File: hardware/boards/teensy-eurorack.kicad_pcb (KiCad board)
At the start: 2 copper layers, 64.8 x 109.2 mm, 52 parts, among them J1 Conn_01x03, J2 Conn_01x02, J27 Conn_01x02, J28 Conn_02x08_Odd_Even, J3 Conn_01x03, U2 AD5754BREZ, U3 AD5754BREZ, U4 Teensy4.1, U5 MCP1700-2502E, U6 AD7606BSTZ, U7 6N138

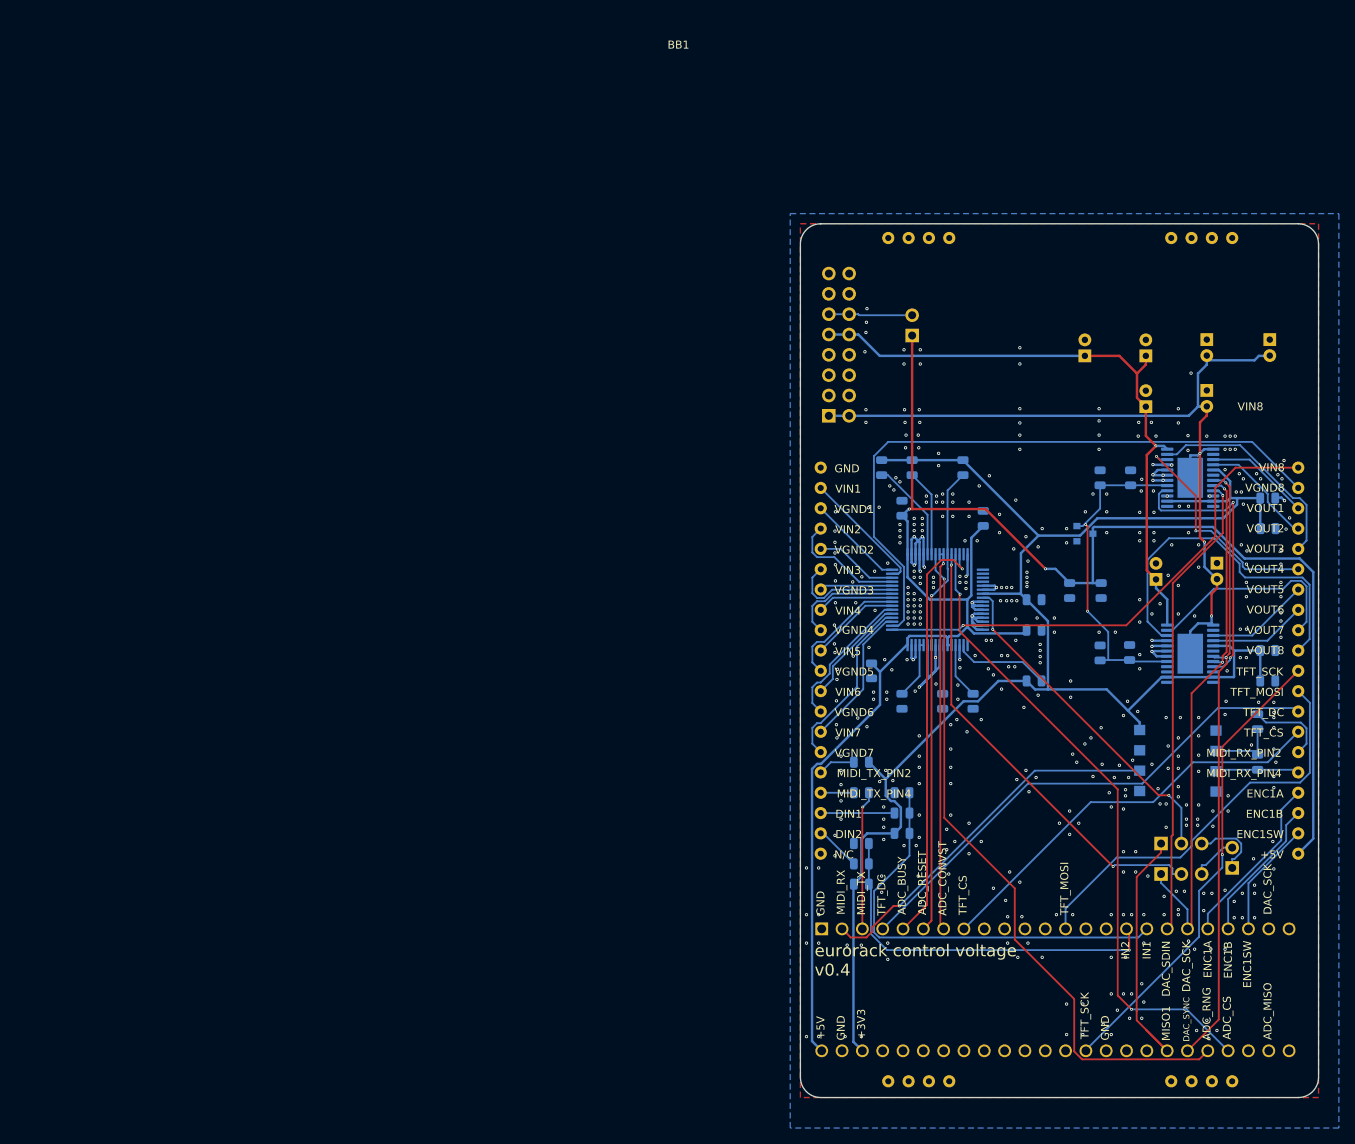
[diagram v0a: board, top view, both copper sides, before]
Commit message: Added jlcpcb parts and changed PCB to 10HP
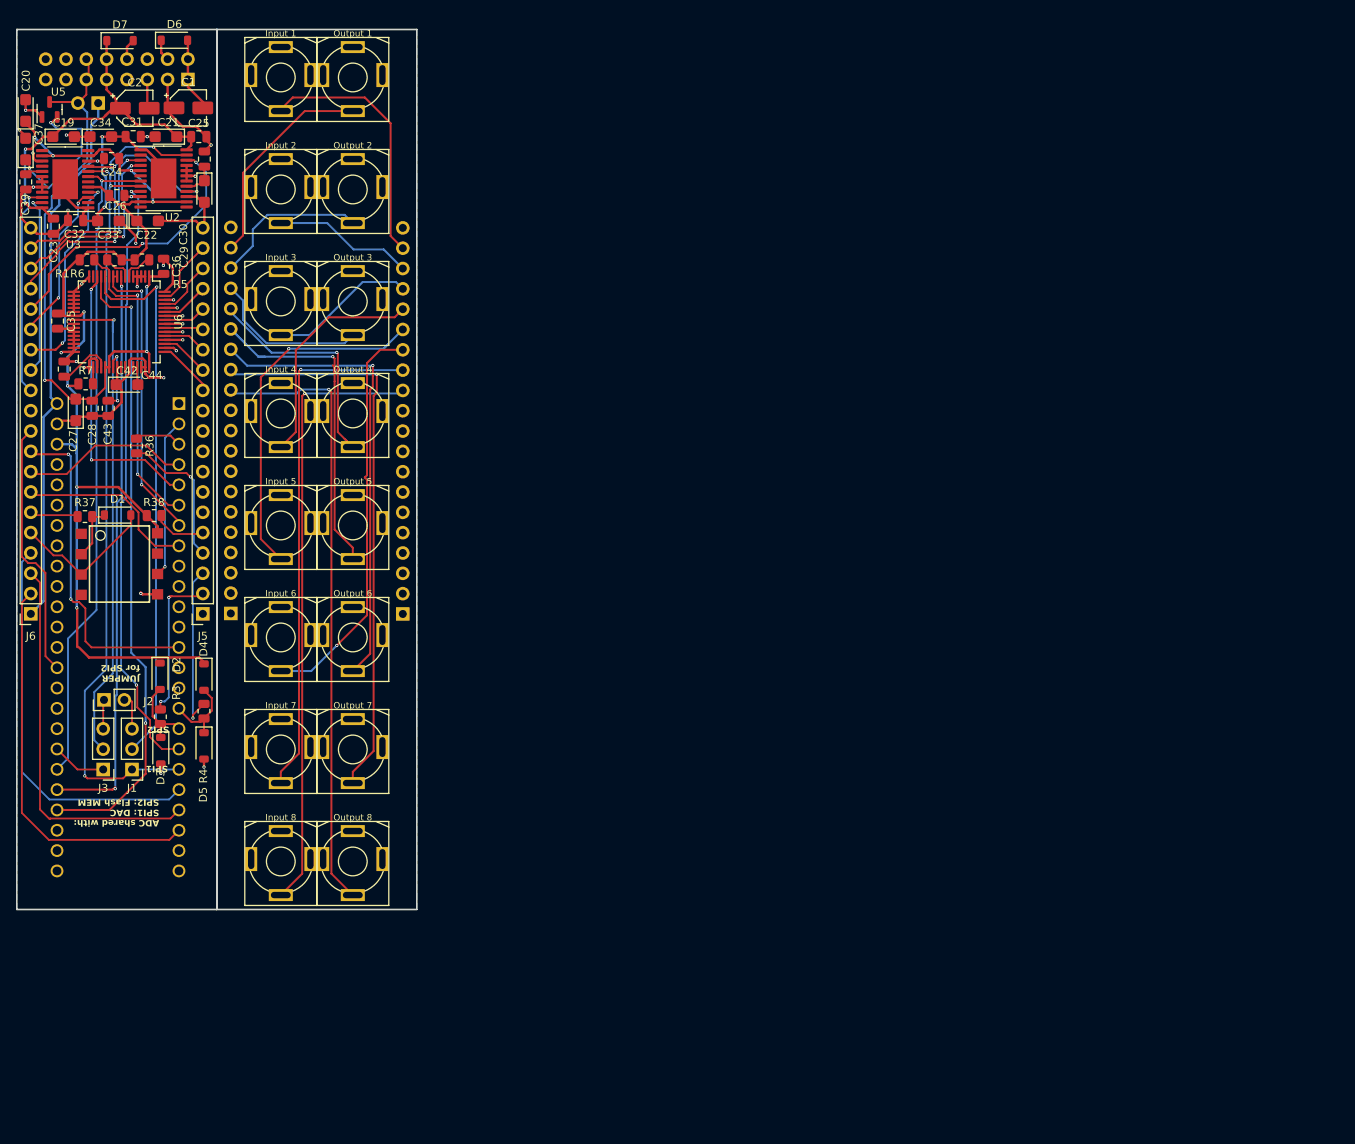
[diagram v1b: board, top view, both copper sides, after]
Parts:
- removed BB1: TEL-breakout, footprints:TElite-breakout-board
- removed C38, C40, C41: 0.1u, Capacitor_SMD:C_0805_2012Metric
- added C1: 10uF, Capacitor_SMD:CP_Elec_4x5.4, F.Cu at (31.4, 19.8)
- added C2: 10uF, Capacitor_SMD:CP_Elec_4x5.4, F.Cu at (24.8, 19.9)
- added D6: 1N5819HW, Diode_SMD:D_SOD-123, F.Cu at (29.7, 11.4)
- added D7: 1N5819HW, Diode_SMD:D_SOD-123, F.Cu at (22.9, 11.4)
- added J10: Input 1, Custom_Footprints:Cliff_3.5mm_Stereo_Jack, F.Cu at (43.0, 16.0)
- added J11: Input 2, Custom_Footprints:Cliff_3.5mm_Stereo_Jack, F.Cu at (43.0, 30.0)
- added J12: Input 3, Custom_Footprints:Cliff_3.5mm_Stereo_Jack, F.Cu at (43.0, 44.0)
- added J13: Input 4, Custom_Footprints:Cliff_3.5mm_Stereo_Jack, F.Cu at (43.0, 58.0)
- added J14: Input 5, Custom_Footprints:Cliff_3.5mm_Stereo_Jack, F.Cu at (43.0, 72.0)
- added J15: Input 6, Custom_Footprints:Cliff_3.5mm_Stereo_Jack, F.Cu at (43.0, 86.0)
- added J16: Input 7, Custom_Footprints:Cliff_3.5mm_Stereo_Jack, F.Cu at (43.0, 100.0)
- added J17: Input 8, Custom_Footprints:Cliff_3.5mm_Stereo_Jack, F.Cu at (43.0, 114.0)
- added J18: Output 1, Custom_Footprints:Cliff_3.5mm_Stereo_Jack, F.Cu at (52.0, 16.0)
- added J19: Output 2, Custom_Footprints:Cliff_3.5mm_Stereo_Jack, F.Cu at (52.0, 30.0)
- added J20: Output 3, Custom_Footprints:Cliff_3.5mm_Stereo_Jack, F.Cu at (52.0, 44.0)
- added J21: Output 4, Custom_Footprints:Cliff_3.5mm_Stereo_Jack, F.Cu at (52.0, 58.0)
- added J22: Output 5, Custom_Footprints:Cliff_3.5mm_Stereo_Jack, F.Cu at (52.0, 72.0)
- added J23: Output 6, Custom_Footprints:Cliff_3.5mm_Stereo_Jack, F.Cu at (52.0, 86.0)
- added J24: Output 7, Custom_Footprints:Cliff_3.5mm_Stereo_Jack, F.Cu at (52.0, 100.0)
- added J25: Output 8, Custom_Footprints:Cliff_3.5mm_Stereo_Jack, F.Cu at (52.0, 114.0)
- added J4: Conn_01x20_Pin, Connector_PinHeader_2.54mm:PinHeader_1x20_P2.54mm_Vertical, B.Cu at (36.8, 83.0)
- added J5: Conn_01x20_Socket, Connector_PinSocket_2.54mm:PinSocket_1x20_P2.54mm_Vertical, F.Cu at (33.2, 83.1)
- added J6: Conn_01x20_Socket, Connector_PinSocket_2.54mm:PinSocket_1x20_P2.54mm_Vertical, F.Cu at (11.8, 83.1)
- added J7: Conn_01x20_Pin, Connector_PinHeader_2.54mm:PinHeader_1x20_P2.54mm_Vertical, B.Cu at (58.2, 83.1)
- C19, C21, C33, C34: footprint Capacitors_THT:CP_Radial_D5.0mm_P2.00mm -> Capacitor_Tantalum_SMD:CP_EIA-3216-10_Kemet-I; moved to F.Cu
- C20, C22, C27, C29, C37, C42: footprint Capacitor_SMD:C_0805_2012Metric -> Capacitor_Tantalum_SMD:CP_EIA-3216-10_Kemet-I; moved to F.Cu
- C23, C25, C31, C32: footprint Capacitors_THT:CP_Radial_D5.0mm_P2.00mm -> Capacitor_SMD:C_0805_2012Metric; moved to F.Cu
- C24, C26, C28, C30, C35, C36, C39, C43, C44, R1, R3, R36, R37, R38, R4, R5, R6, R7, U2, U3, U5, U6, U7: moved to F.Cu
- D1, D2, D3, D4, D5: footprint Diode_SMD:D_0805_2012Metric -> Diode_SMD:D_SOD-123; moved to F.Cu
- J1, J3: value Conn_01x03 -> Conn_01x03_Pin; footprint Pin_Headers:Pin_Header_Straight_1x03_Pitch2.54mm -> Connector_PinHeader_2.54mm:PinHeader_1x03_P2.54mm_Vertical; moved to F.Cu
- J2: value Conn_01x02 -> Conn_01x02_Pin; footprint Pin_Headers:Pin_Header_Straight_1x02_Pitch2.54mm -> Connector_PinHeader_2.54mm:PinHeader_1x02_P2.54mm_Vertical; moved to F.Cu
- J28: footprint Connector_PinHeader_2.54mm:PinHeader_2x08_P2.54mm_Vertical -> Custom_Footprints:Eurorack_16_pin_header
- moved C20 170.9 mm to (11.1, 20.1), turned to 90 degrees
- moved C24 157.1 mm to (21.9, 26.1), turned to 180 degrees
- moved U3 152.6 mm to (16.1, 28.7)
- moved C39 150.0 mm to (11.1, 29.1), turned to -90 degrees
- moved C26 149.8 mm to (22.5, 30.8)
- moved C32 149.0 mm to (17.4, 33.9), turned to 0 degrees
- moved R37 148.8 mm to (18.5, 70.9), turned to 180 degrees
- moved C33 145.9 mm to (21.4, 33.9), turned to 180 degrees
- moved D1 145.8 mm to (22.6, 70.7), turned to 0 degrees
- moved C23 144.7 mm to (14.6, 34.6), turned to -90 degrees
- moved C22 144.2 mm to (26.4, 33.9)
- moved J2 142.6 mm to (20.9, 93.8), turned to 90 degrees
- moved C34 140.6 mm to (20.5, 23.4), turned to 0 degrees
- moved C37 140.5 mm to (11.1, 25.0)
- moved U5 139.9 mm to (14.1, 20.0), turned to 90 degrees
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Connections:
- C27 pad 2: +5V -> +5VA
- C28 pad 2: +5V -> +5VA
- C36 pad 1: +5V -> +5VA
- D2 pad 2: /IN2 -> /_IN2
- D3 pad 1: /IN2 -> /_IN2
- D4 pad 2: /IN1 -> /_IN1
- D5 pad 1: /IN1 -> /_IN1
- J27 pad 2: Net-(J27-Pad2) -> +5VA
- J28 pad 11: Net-(J27-Pad2) -> +5VA
- J28 pad 12: Net-(J27-Pad2) -> +5VA
- J28 pad 13: Net-(J28-Pad13) -> unconnected-(J28-Pin_13-Pad13)
- J28 pad 14: Net-(J28-Pad14) -> unconnected-(J28-Pin_14-Pad14)
- J28 pad 15: Net-(J28-Pad15) -> unconnected-(J28-Pin_15-Pad15)
- J28 pad 16: Net-(J28-Pad16) -> unconnected-(J28-Pin_16-Pad16)
- R3 pad 1: /IN2 -> /_IN2
- R4 pad 1: /IN1 -> /_IN1
- U2 pad 12: Net-(U2-Pad12) -> unconnected-(U2-1_NC-Pad12)
- U2 pad 13: Net-(U2-Pad13) -> unconnected-(U2-2_NC-Pad13)
- U2 pad 2: Net-(U2-Pad2) -> unconnected-(U2-3_NC-Pad2)
- U2 pad 6: Net-(U2-Pad6) -> unconnected-(U2-4_NC-Pad6)
- U3 pad 12: Net-(U3-Pad12) -> unconnected-(U3-1_NC-Pad12)
- U3 pad 13: Net-(U3-Pad13) -> unconnected-(U3-2_NC-Pad13)
- U3 pad 16: Net-(U3-Pad16) -> unconnected-(U3-SDO-Pad16)
- U3 pad 2: Net-(U3-Pad2) -> unconnected-(U3-3_NC-Pad2)
- U3 pad 6: Net-(U3-Pad6) -> unconnected-(U3-4_NC-Pad6)
- U4 pad 10: Net-(U4-Pad10) -> unconnected-(U4-8_TX2_IN1-Pad10)
- U4 pad 11: Net-(U4-Pad11) -> unconnected-(U4-9_OUT1C-Pad11)
- U4 pad 12: Net-(U4-Pad12) -> unconnected-(U4-10_CS_MQSR-Pad12)
- U4 pad 14: Net-(U4-Pad14) -> unconnected-(U4-12_MISO_MQSL-Pad14)
- U4 pad 15: Net-(U4-Pad15) -> unconnected-(U4-3V3-Pad15)
- U4 pad 16: /IN2 -> /_IN1
- U4 pad 17: /IN1 -> /_IN2
- U4 pad 23: Net-(U4-Pad23) -> unconnected-(U4-31_CTX3-Pad23)
- U4 pad 24: Net-(U4-Pad24) -> unconnected-(U4-32_OUT1B-Pad24)
- U4 pad 25: Net-(U4-Pad25) -> unconnected-(U4-33_MCLK2-Pad25)
- U4 pad 26: Net-(U4-Pad26) -> unconnected-(U4-34-Pad26)
- U4 pad 27: Net-(U4-Pad27) -> unconnected-(U4-35-Pad27)
- U4 pad 32: Net-(U4-Pad32) -> unconnected-(U4-40-Pad32)
- U4 pad 33: Net-(U4-Pad33) -> unconnected-(U4-41-Pad33)
- U4 pad 36: Net-(U4-Pad36) -> unconnected-(U4-14_A0_TX3_SPDIF_OUT-Pad36)
- U4 pad 37: Net-(U4-Pad37) -> unconnected-(U4-15_A1_RX3_SPDIF_IN-Pad37)
- U4 pad 38: Net-(U4-Pad38) -> unconnected-(U4-16_A2_RX4_SCL1-Pad38)
- U4 pad 39: Net-(U4-Pad39) -> unconnected-(U4-17_A3_TX4_SDA1-Pad39)
- U4 pad 40: Net-(U4-Pad40) -> unconnected-(U4-18_A4_SDA0-Pad40)
- U4 pad 41: Net-(U4-Pad41) -> unconnected-(U4-19_A5_SCL0-Pad41)
- U4 pad 42: Net-(U4-Pad42) -> unconnected-(U4-20_A6_TX5_LRCLK1-Pad42)
- U4 pad 43: Net-(U4-Pad43) -> unconnected-(U4-21_A7_RX5_BCLK1-Pad43)
- U4 pad 44: Net-(U4-Pad44) -> unconnected-(U4-22_A8_CTX1-Pad44)
- U4 pad 45: Net-(U4-Pad45) -> unconnected-(U4-23_A9_CRX1_MCLK1-Pad45)
- U4 pad 9: Net-(U4-Pad9) -> unconnected-(U4-7_RX2_OUT1A-Pad9)
- U5 pad 3: +5V -> +5VA
- U6 pad 1: +5V -> +5VA
- U6 pad 15: Net-(U6-Pad15) -> unconnected-(U6-FRSTDATA-Pad15)
- U6 pad 37: +5V -> +5VA
- U6 pad 38: +5V -> +5VA
- U6 pad 42: Net-(U6-Pad42) -> unconnected-(U6-REFIN/REFOUT-Pad42)
- U6 pad 48: +5V -> +5VA
- U6 pad 50: /VGND8 -> GND
- U6 pad 52: /VGND7 -> GND
- U6 pad 54: /VGND6 -> GND
- U6 pad 56: /VGND5 -> GND
- U6 pad 58: /VGND4 -> GND
- U6 pad 60: /VGND3 -> GND
- U6 pad 62: /VGND2 -> GND
- U6 pad 64: /VGND1 -> GND
- U7 pad 1: Net-(U7-Pad1) -> unconnected-(U7-NC-Pad1)
- U7 pad 4: Net-(U7-Pad4) -> unconnected-(U7-NC-Pad4)
- U7 pad 7: Net-(U7-Pad7) -> unconnected-(U7-VO1-Pad7)
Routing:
- net +5V: track 230.1 -> 68.0 mm, vias 2 -> 0
- net /VGND8: track 80.0 -> 0.00 mm
- net +5VA: track 0.00 -> 77.5 mm, vias 0 -> 3
- net /OUT8: track 0.00 -> 77.1 mm, vias 0 -> 1
- net /IN8: track 0.00 -> 76.3 mm, vias 0 -> 1
- net /OUT7: track 0.00 -> 70.8 mm, vias 0 -> 1
- net +3V3: track 208.5 -> 141.9 mm, vias 0 -> 8
- net -12V: track 103.2 -> 36.8 mm, vias 3 -> 2
- net /IN7: track 0.00 -> 65.5 mm, vias 0 -> 1
- net GND: track 77.2 -> 139.2 mm, vias 463 -> 29
- net /OUT6: track 0.00 -> 57.8 mm, vias 0 -> 1
- net /VIN8: track 62.7 -> 7.24 mm, vias 1 -> 0
- net /IN6: track 0.00 -> 50.6 mm, vias 0 -> 1
- net /OUT5: track 0.00 -> 45.1 mm, vias 0 -> 1
- net /IN5: track 0.00 -> 44.8 mm, vias 0 -> 1
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- removed copper zone on F.Cu, net GND
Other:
- board size 64.8 x 109.2 mm -> 50 x 110 mm
- net class Default removed
- net class PWR removed
- board text added: "ADC shared with: SPI1: DAC SPI2: Flash MEM"
- board text added: "JUMPER for SPI2"
- board text added: "Remove jumper for Teensy USB"
- board text removed: "+3V3"
- board text removed: "+5V"
- board text removed: "ADC_BUSY"
- board text removed: "ADC_CONVST"
- board text removed: "ADC_CS"
- board text removed: "ADC_MISO"
- board text removed: "ADC_RESET"
- board text removed: "ADC_RNG"
- board text removed: "DAC_SCK"
- board text removed: "DAC_SDIN"
- board text removed: "DAC_SYNC"
- board text removed: "DIN1"
- board text removed: "DIN2"
- board text removed: "ENC1A"
- board text removed: "ENC1B"
- board text removed: "ENC1SW"
- board text removed: "Eurorack power bus"
- board text removed: "GND"
- board text removed: "IN1"
- board text removed: "IN2"
- board text removed: "J1, J3: Select SPI1 for ADC to use SPI1 (share with DAC) Select SPI2 for ADC to use SPI2 (share with flash)"
- board text removed: "J2: if you are using SPI2 for ADC: connect MISO2 to pin 54 connect SCK2 to pin 49 (on underneath teensy 4.1)"
- board text removed: "MIDI_RX"
- board text removed: "MIDI_RX_PIN2"
- board text removed: "MIDI_RX_PIN4"
- board text removed: "MIDI_TX"
- board text removed: "MIDI_TX_PIN2"
- board text removed: "MIDI_TX_PIN4"
- board text removed: "MISO1"
- board text removed: "N/C"
- board text removed: "PIN 1"
- board text removed: "TFT_CS"
- board text removed: "TFT_DC"
- board text removed: "TFT_MOSI"
- board text removed: "TFT_SCK"
- board text removed: "VGND1"
- board text removed: "VGND2"
- board text removed: "VGND3"
- board text removed: "VGND4"
- board text removed: "VGND5"
- board text removed: "VGND6"
- board text removed: "VGND7"
- board text removed: "VGND8"
- board text removed: "VIN1"
- board text removed: "VIN2"
- board text removed: "VIN3"
- board text removed: "VIN4"
- board text removed: "VIN5"
- board text removed: "VIN6"
- board text removed: "VIN7"
- board text removed: "VIN8"
- board text removed: "VOUT1"
- board text removed: "VOUT2"
- board text removed: "VOUT3"
- board text removed: "VOUT4"
- board text removed: "VOUT5"
- board text removed: "VOUT6"
- board text removed: "VOUT7"
- board text removed: "VOUT8"
- board text removed: "connect jumper J27 to power from eurorack power bus 5v CAUTION: Do not connect teensy to host while using eurorack power."
- board text removed: "eurorack control voltage v0.4"
- board text removed: "https://github.com/newdigate/teensy-control-voltage version 0.4"
